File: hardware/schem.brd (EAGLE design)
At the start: 42.9 x 29.2 mm, 8 parts

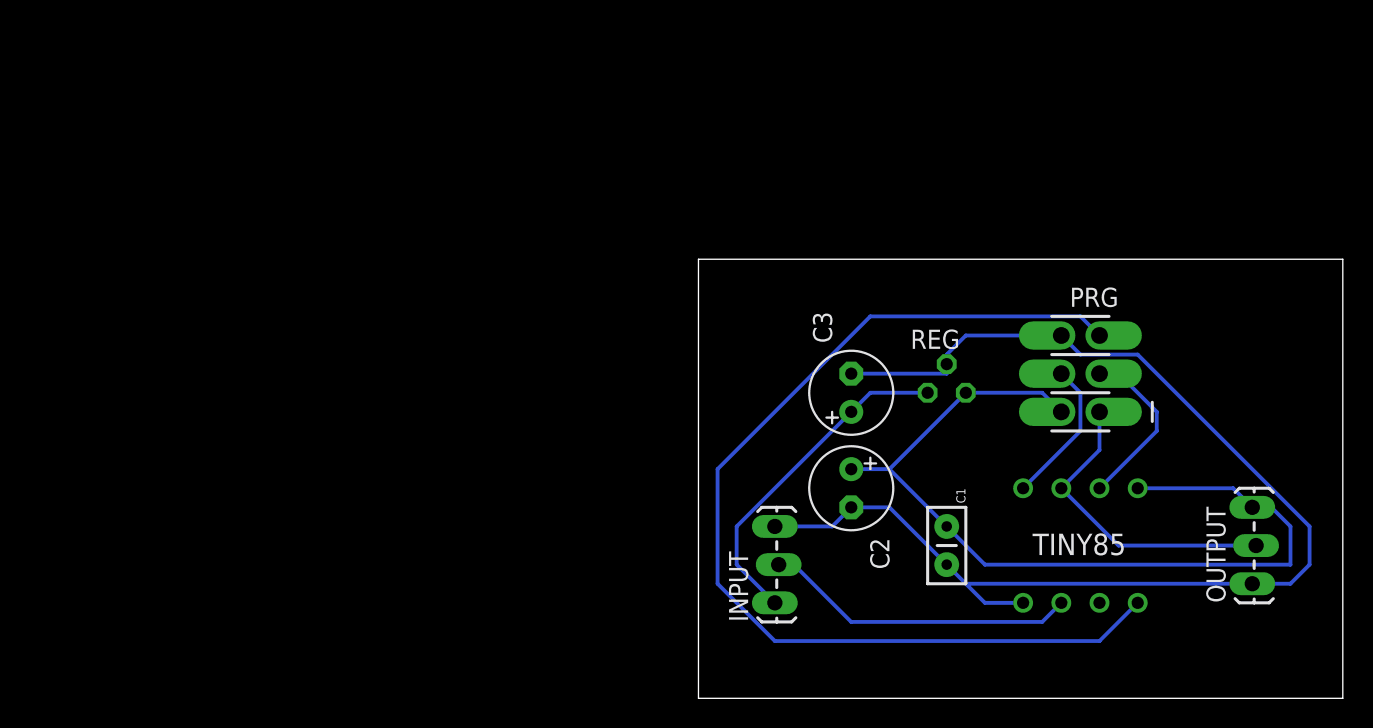
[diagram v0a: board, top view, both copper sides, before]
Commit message: Updated Schematic to use integrated H Bridge with DC Motor
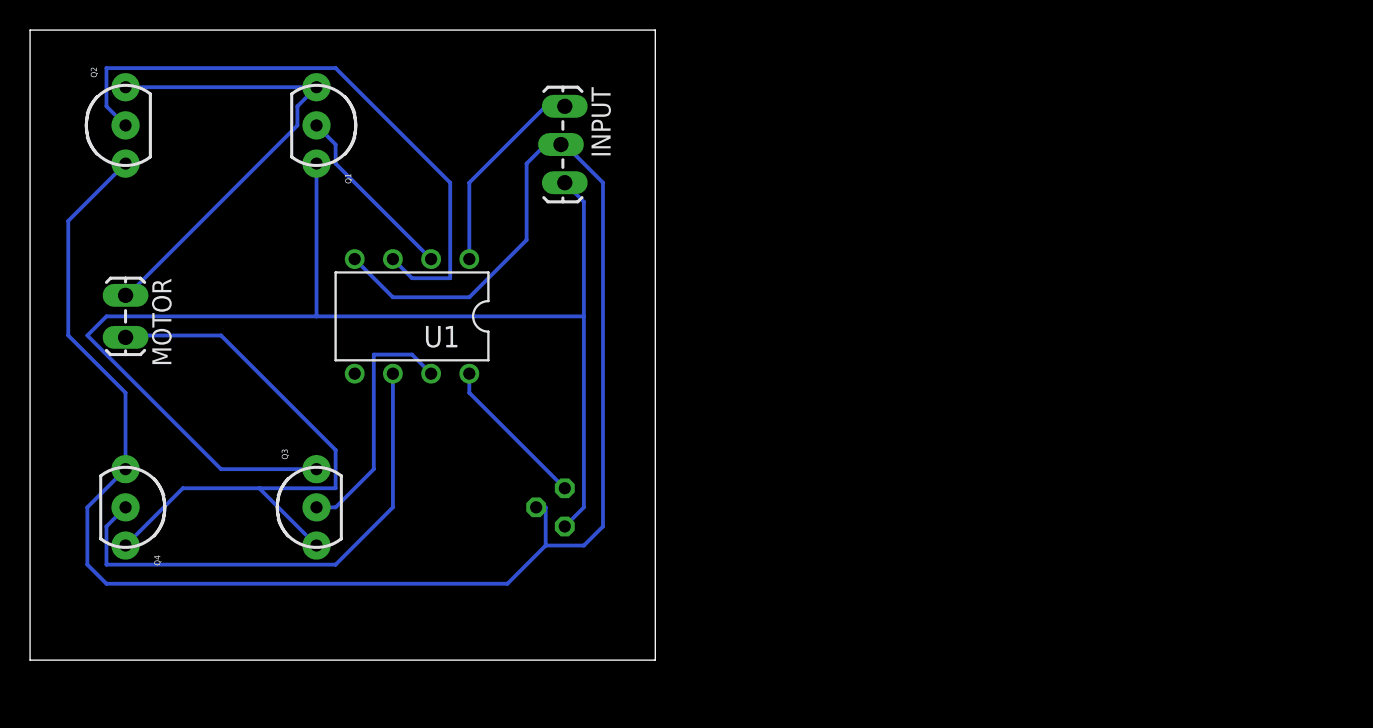
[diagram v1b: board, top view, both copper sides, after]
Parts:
- removed C1: 10n, SparkFun-Capacitors:CAP-PTH-SMALLEZ
- removed C2, C3: 10u, rcl:E2,5-6
- removed OUTPUT: (no value), SparkFun-Connectors:1X03_LOCK_LONGPADS
- removed PRG: AVR_SPI_PRG_6OFFSET_PADS, SparkFun-Connectors:2X3_OFFSET
- removed REG: 7805L, linear:TO92
- removed TINY85: ATTINY85-P, _hhn_attiny25_45_85:PDIP08_300MIL
- added IC1: 7805L, linear:TO92
- added MOTOR: M02LOCK_LONGPADS, SparkFun-Connectors:1X02_LOCK_LONGPADS
- added Q1, Q2, Q3, Q4: (no value), SparkFun-DiscreteSemi:TO-92-AMMO
- added U1: ATTINY85-P, _hhn_attiny25_45_85:PDIP08_300MIL
- moved INPUT 35.9 mm to (53.3, 69.8), turned to 270 degrees
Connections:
- new net N$1: MOTOR.1, Q1.1, Q2.3
- new net N$10: IC1.1, U1.8
- net N$2: now also MOTOR.2, Q3.1, Q4.3; no longer PRG.3, TINY85.7
- net N$3: now also INPUT.1, U1.1; no longer PRG.5, TINY85.1
- net N$4: now also Q1.2, U1.2; no longer PRG.4, TINY85.5
- net N$5: now also IC1.3, INPUT.3, Q1.3, Q3.3; no longer OUTPUT.2, PRG.1, TINY85.6
- net N$6: now also IC1.2, Q2.1, Q4.1, U1.4; no longer TINY85.3
- net N$7: now also Q2.2, U1.3; no longer C3.+, INPUT.1, REG.3
- net N$8: now also Q4.2, U1.6; no longer C1.1, C2.+, OUTPUT.3, PRG.2, REG.1, TINY85.8
- net N$9: now also Q3.2, U1.7; no longer C1.2, C2.-, C3.-, INPUT.3, OUTPUT.1, PRG.6, REG.2, TINY85.4
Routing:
- net N$6: track 20.9 -> 119.1 mm
- net N$9: track 83.1 -> 16.8 mm
- net N$5: track 20.7 -> 86.5 mm
- net N$3: track 68.3 -> 13.5 mm
- net N$1: track 0.00 -> 32.1 mm
- net N$2: track 11.5 -> 40.7 mm
- net N$8: track 59.7 -> 33.9 mm
- net N$7: track 22.5 -> 41.0 mm
- net N$10: track 0.00 -> 10.3 mm
- net N$4: track 9.72 -> 12.0 mm
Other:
- board size 42.9 x 29.2 mm -> 41.6 x 41.9 mm

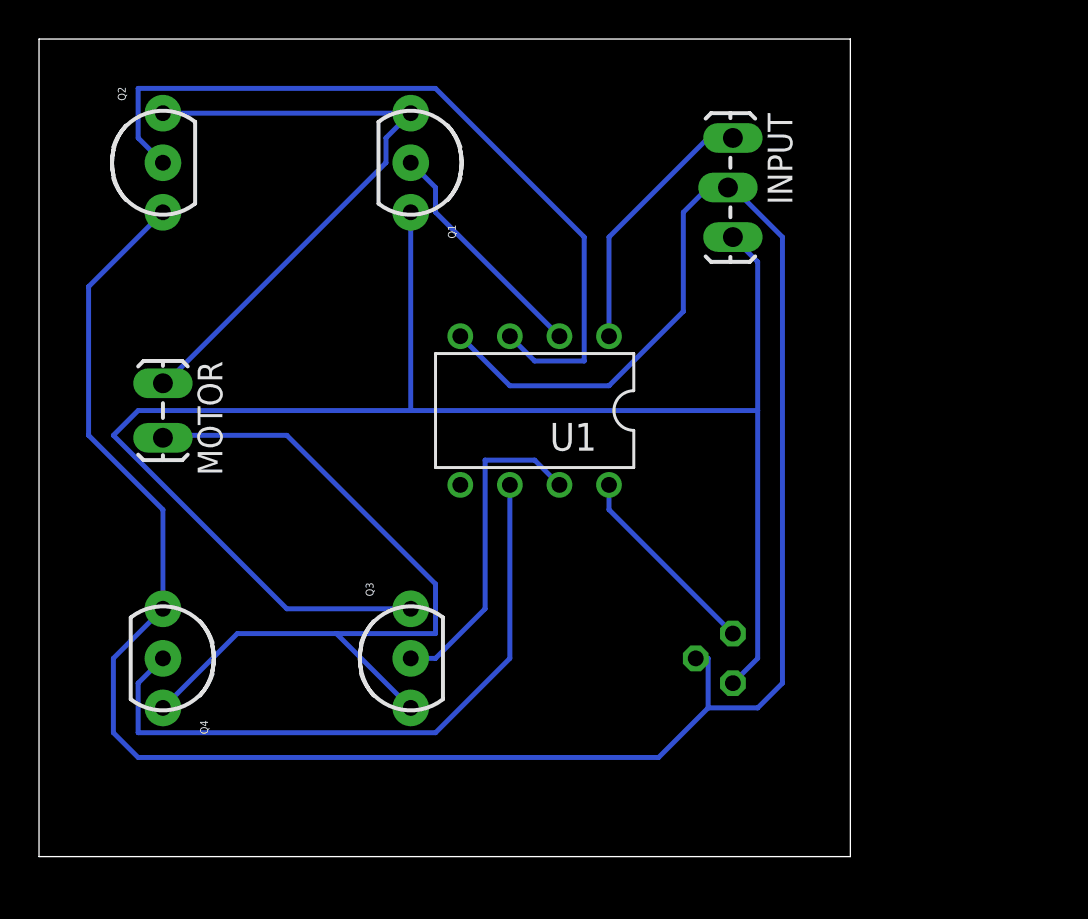
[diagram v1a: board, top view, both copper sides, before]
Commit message: Updated Schematic and Board to include AVR ISP Header
Changed the structure of the H Bridge as well. No longer are you able to independently control all 4 "switches". Now, you control the motor with tow pins (forward or reverse). Layout has yet to bo optimized.
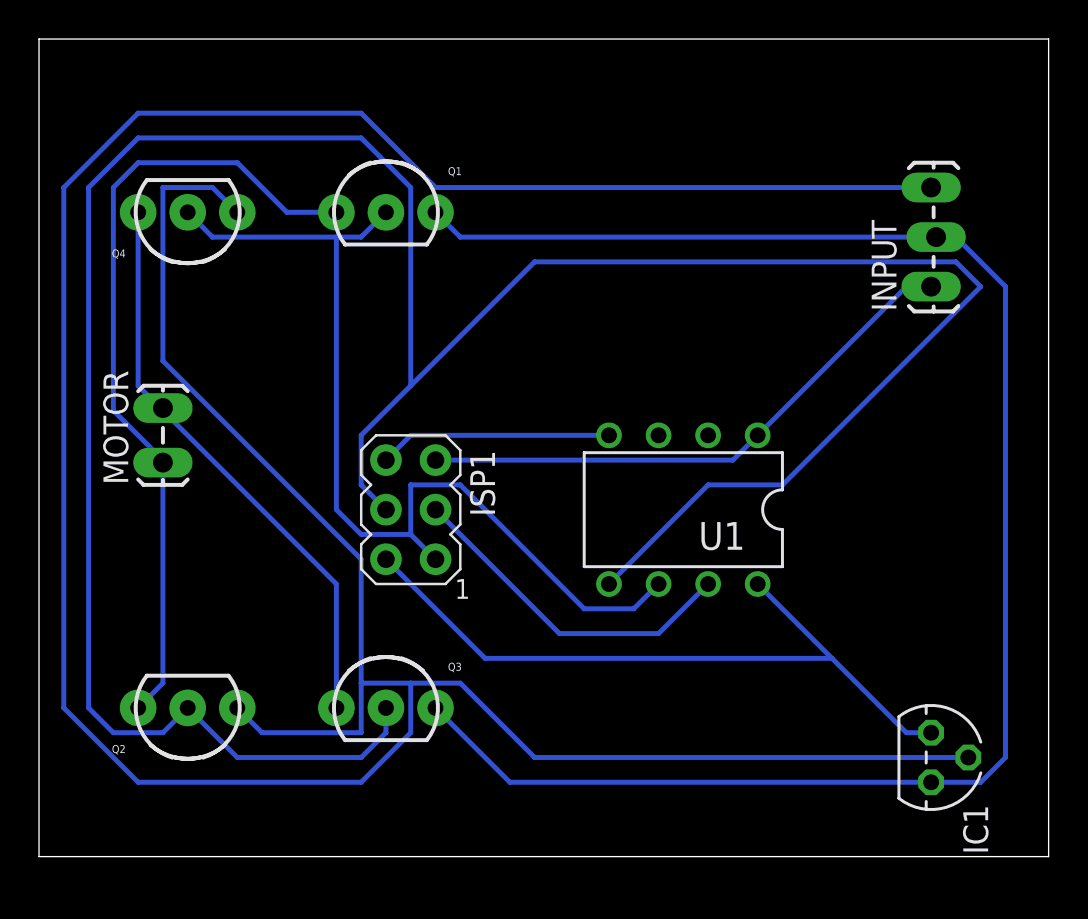
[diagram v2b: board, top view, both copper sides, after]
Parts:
- added ISP1: AVRISP-6, adafruit:AVRISP
- moved Q2 28.0 mm to (25.4, 40.6), turned to 180 degrees
- moved Q4 22.9 mm to (25.4, 66.0), turned to 180 degrees
- moved INPUT 12.7 mm to (63.5, 62.2), turned to 90 degrees
- moved IC1 11.4 mm to (63.5, 38.1), flipped to the top
- moved U1 9.16 mm to (50.8, 50.8)
- moved MOTOR 3.81 mm to (24.1, 53.3), turned to 90 degrees
- moved Q3 2.84 mm to (35.6, 40.6), turned to 0 degrees
- moved Q1 2.84 mm to (35.6, 66.0), turned to 0 degrees
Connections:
- net N$10: now also ISP1.3, U1.7; no longer IC1.1, U1.8
- net N$3: now also IC1.2, INPUT.3, Q2.1, Q4.1; no longer INPUT.1, U1.1
- net N$4: now also IC1.3, INPUT.2, Q1.3, Q3.3; no longer Q1.2, U1.2
- net N$5: now also ISP1.1, Q1.2, Q4.2, U1.6; no longer IC1.3, INPUT.3, Q1.3, Q3.3
- net N$6: now also ISP1.6; no longer IC1.2, INPUT.2, Q2.1, Q4.1
- net N$7: now also IC1.1, ISP1.2, U1.8; no longer Q2.2, U1.3
- net N$8: now also ISP1.4, Q2.2, Q3.2, U1.5; no longer Q4.2, U1.6
- net N$9: now also INPUT.1, ISP1.5, U1.1; no longer Q3.2, U1.7
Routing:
- net N$3: track 13.5 -> 173.3 mm
- net N$6: track 119.1 -> 12.0 mm
- net N$8: track 33.9 -> 140.2 mm
- net N$4: track 12.0 -> 86.2 mm
- net N$5: track 86.5 -> 49.7 mm
- net N$9: track 16.8 -> 29.1 mm
- net N$2: track 40.7 -> 29.7 mm
- net N$1: track 32.1 -> 41.3 mm
- net N$10: track 10.3 -> 17.7 mm
- net N$7: track 41.0 -> 37.0 mm
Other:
- board size 41.6 x 41.9 mm -> 51.7 x 41.9 mm

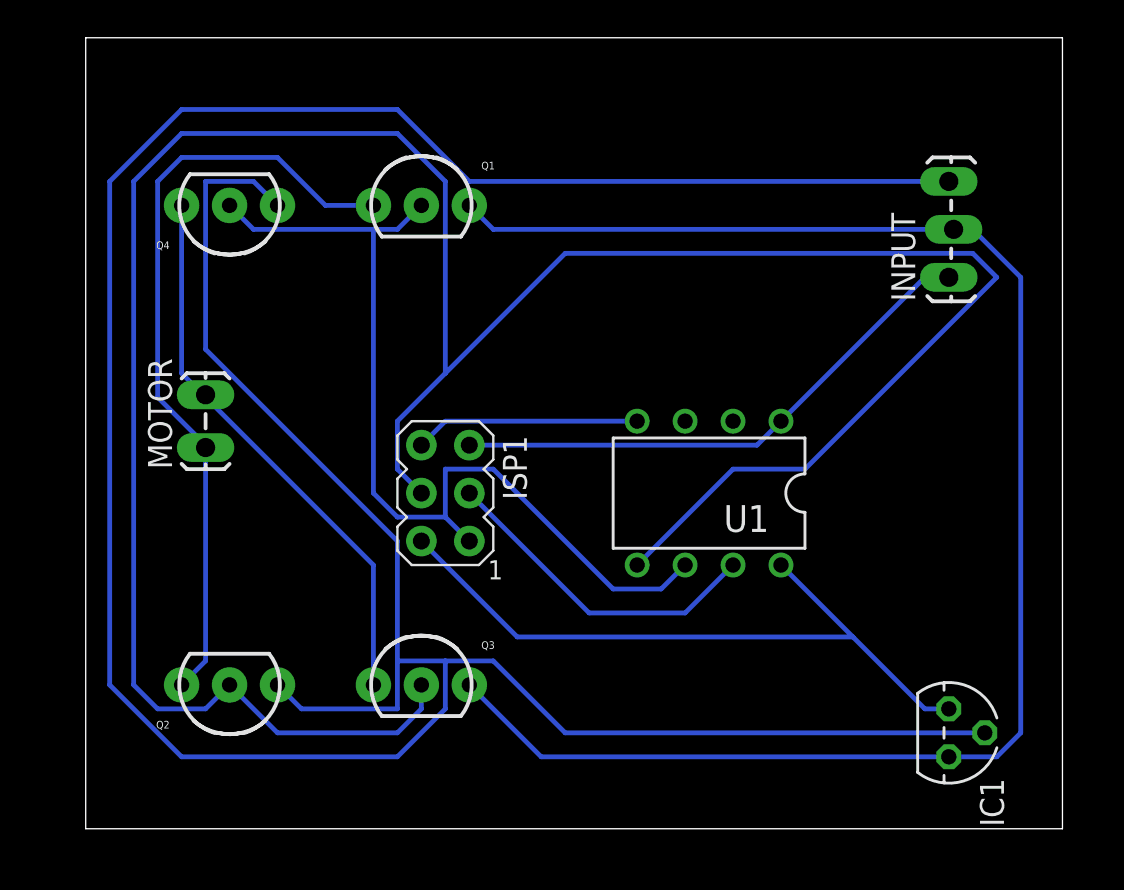
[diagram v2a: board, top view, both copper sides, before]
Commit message: Cleaned up Schematic and fixed transitors
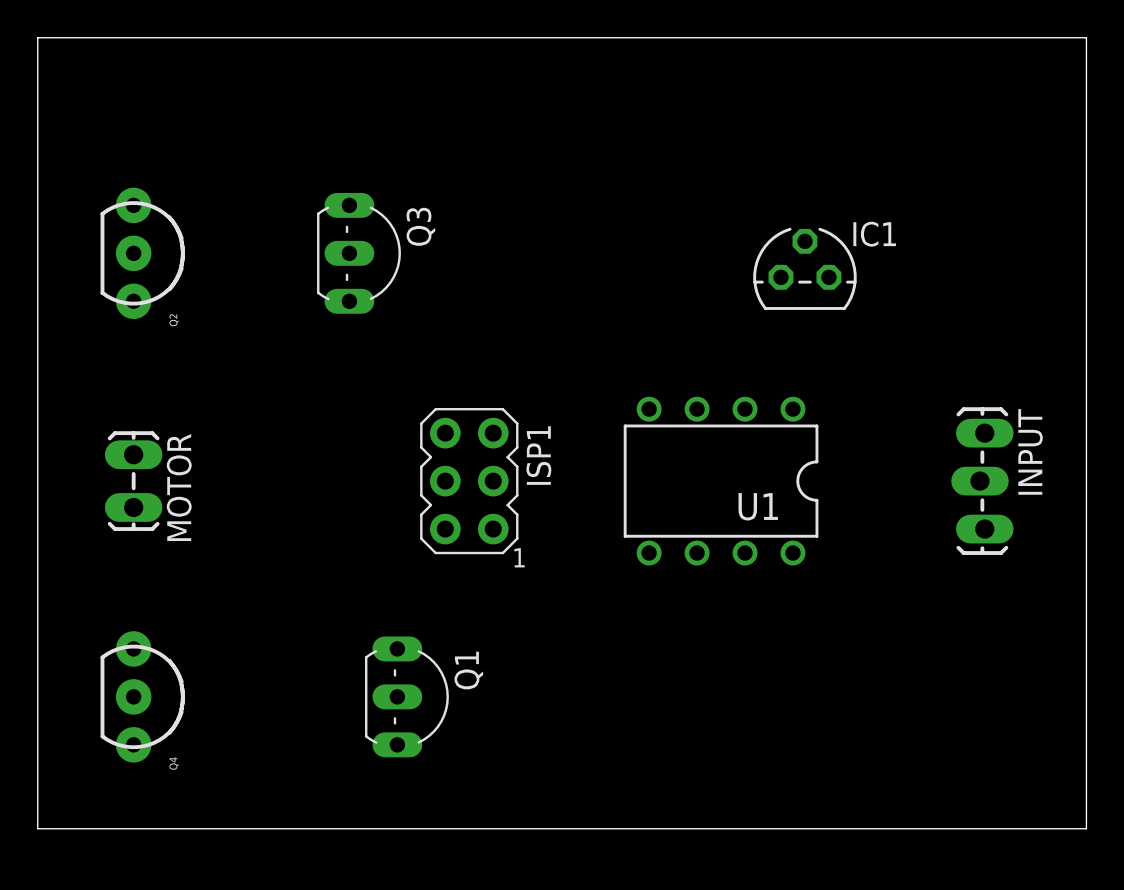
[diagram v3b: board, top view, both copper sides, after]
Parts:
- Q1, Q3: device SparkFun-DiscreteSemi:TO-92-AMMO -> transistor:TO92-EBC
- moved Q4 26.5 mm to (20.3, 40.0), turned to 270 degrees
- moved Q1 26.0 mm to (35.6, 40.0), turned to 270 degrees
- moved IC1 25.3 mm to (55.9, 62.2), turned to 0 degrees
- moved Q2 23.4 mm to (20.3, 63.5), turned to 270 degrees
- moved Q3 23.0 mm to (33.0, 63.5), turned to 270 degrees
- moved INPUT 8.47 mm to (65.4, 54.0), turned to 270 degrees
- moved MOTOR 3.86 mm to (20.3, 52.7), turned to 270 degrees
- moved ISP1 1.42 mm to (38.1, 51.4)
- moved U1 0.90 mm to (51.4, 51.4)
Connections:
- net N$10 renamed SCK
- net N$7 renamed +5V
- removed net N$2: MOTOR.2, Q3.1, Q4.3
- removed net N$3: IC1.2, INPUT.3, Q2.1, Q4.1
- removed net N$4: IC1.3, INPUT.2, Q1.3, Q3.3
- removed net N$5: ISP1.1, Q1.2, Q4.2, U1.6
- removed net N$6: ISP1.6, U1.4
- removed net N$8: ISP1.4, Q2.2, Q3.2, U1.5
- removed net N$9: INPUT.1, ISP1.5, U1.1
- new net +12V: IC1.3, INPUT.3, Q1.E, Q3.E
- new net GND: IC1.2, INPUT.1, ISP1.6, Q2.1, Q4.1, U1.4
- new net INP: INPUT.2, ISP1.5, U1.1
- new net MISO: ISP1.1, U1.6
- new net MOSI: ISP1.4, Q1.B, Q4.2, U1.5
- new net OUT: Q2.2, Q3.B, U1.3
- net N$1: now also MOTOR.2, Q1.C, Q3.C, Q4.3; no longer Q1.1
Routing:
- net N$3: track 173.3 -> 0.00 mm
- net N$8: track 140.2 -> 0.00 mm
- net N$4: track 86.2 -> 0.00 mm
- net N$5: track 49.7 -> 0.00 mm
- net N$1: track 41.3 -> 0.00 mm
- net +5V: track 37.0 -> 0.00 mm
- net N$2: track 29.7 -> 0.00 mm
- net N$9: track 29.1 -> 0.00 mm
- net SCK: track 17.7 -> 0.00 mm
- net N$6: track 12.0 -> 0.00 mm
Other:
- board size 51.7 x 41.9 mm -> 55.6 x 41.9 mm

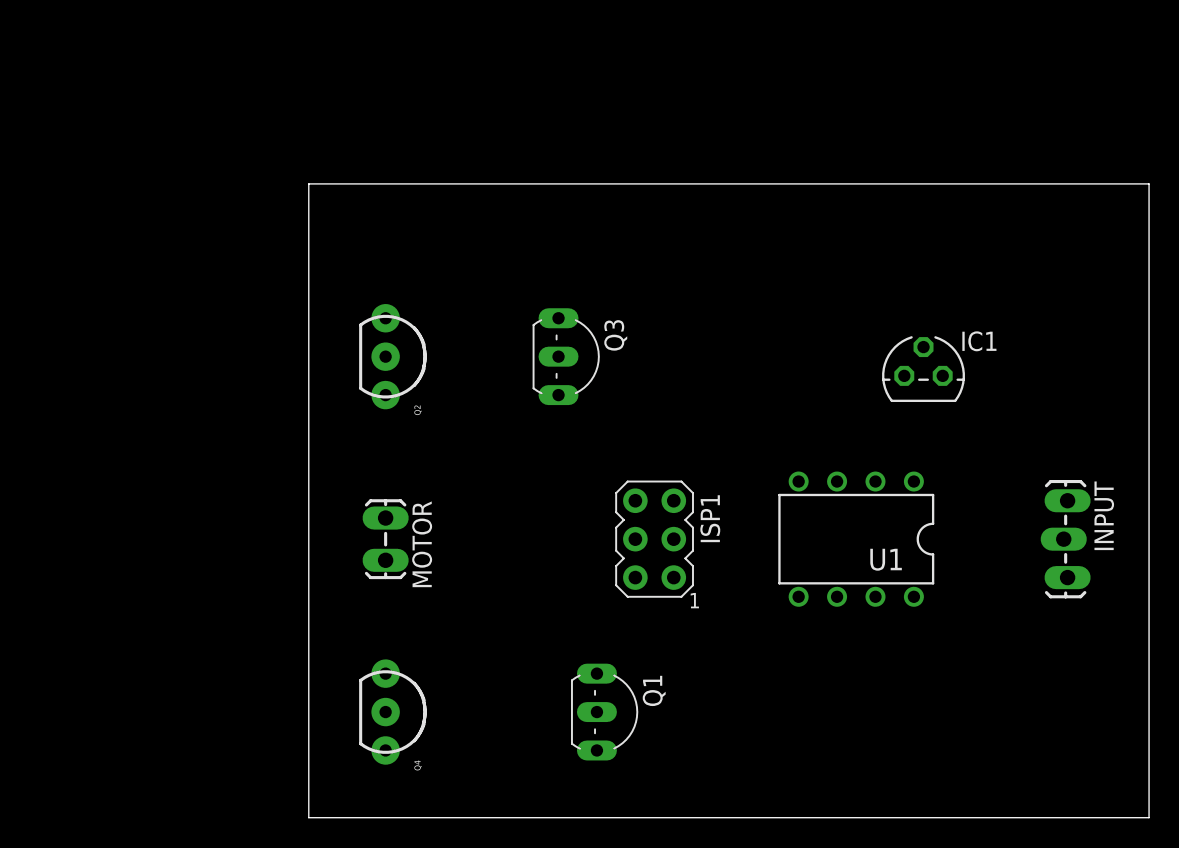
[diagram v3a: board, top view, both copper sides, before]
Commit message: Routed board
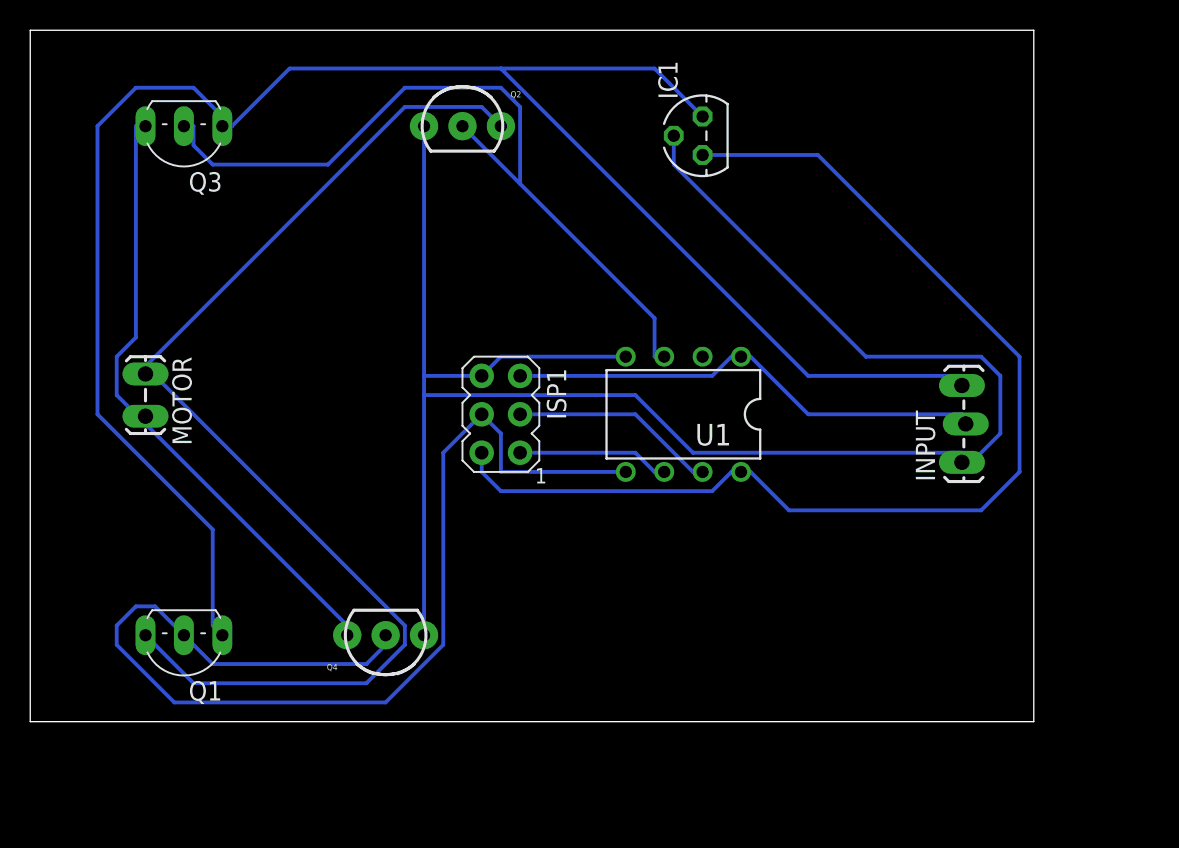
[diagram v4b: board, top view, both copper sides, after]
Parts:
- moved Q3 29.5 mm to (6.99, 77.5), turned to 180 degrees
- moved Q1 28.8 mm to (6.99, 43.8), turned to 180 degrees
- moved IC1 21.6 mm to (41.3, 78.1), turned to 90 degrees
- moved MOTOR 18.5 mm to (4.45, 62.2)
- moved Q2 16.1 mm to (25.4, 78.7), turned to 0 degrees
- moved U1 14.1 mm to (40.0, 59.7)
- moved ISP1 13.1 mm to (27.9, 59.7)
- moved INPUT 7.43 mm to (58.4, 56.5), turned to 90 degrees
- moved Q4 5.08 mm to (20.3, 45.1), turned to 180 degrees
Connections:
- new net N$2: MOTOR.2, Q3.C, Q4.3
- net N$1: no longer MOTOR.2, Q3.C, Q4.3
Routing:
- net GND: track 0.00 -> 122.6 mm
- net +12V: track 0.00 -> 122.2 mm
- net N$1: track 0.00 -> 77.4 mm
- net MOSI: track 0.00 -> 75.9 mm
- net +5V: track 0.00 -> 74.1 mm
- net OUT: track 0.00 -> 52.9 mm
- net N$2: track 0.00 -> 41.8 mm
- net INP: track 0.00 -> 32.0 mm
- net SCK: track 0.00 -> 13.6 mm
- net MISO: track 0.00 -> 10.1 mm
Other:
- board size 55.6 x 41.9 mm -> 66.3 x 45.7 mm
